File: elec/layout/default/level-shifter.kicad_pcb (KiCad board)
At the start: 2 copper layers, 225.7 x 100.8 mm, 0 parts

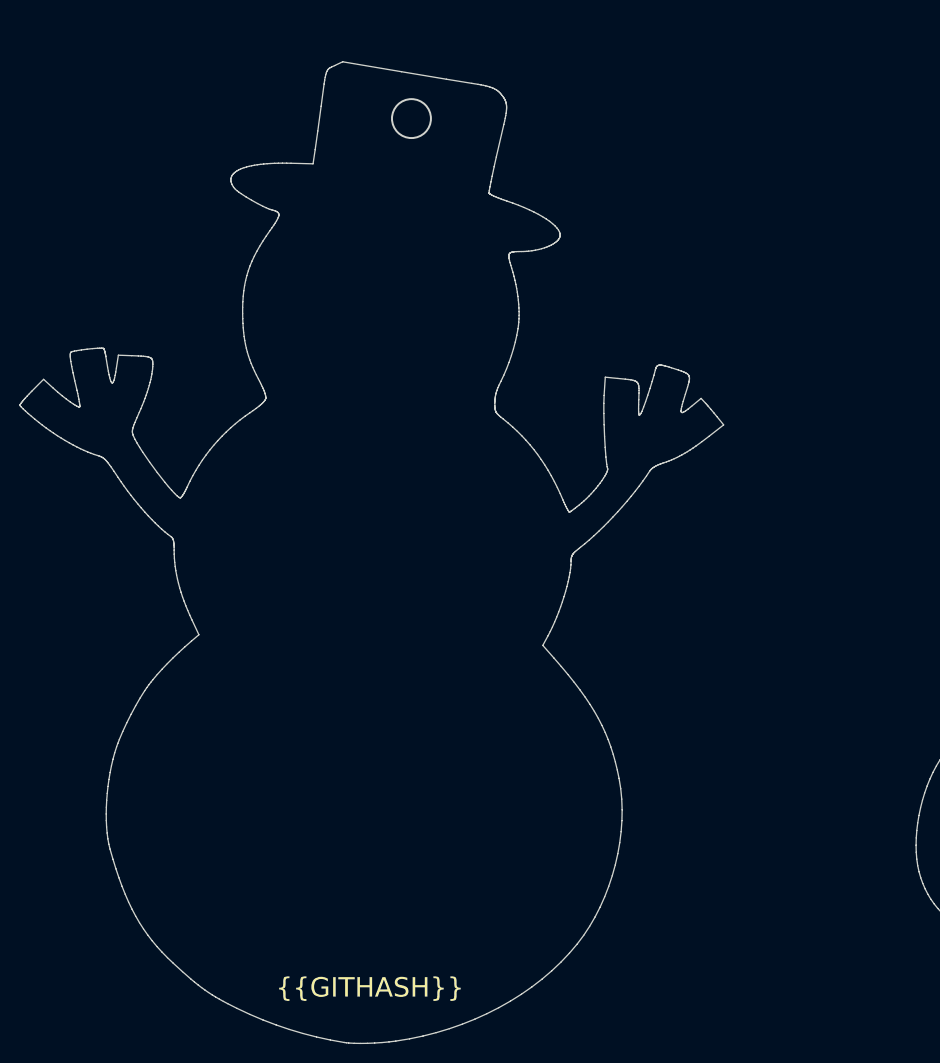
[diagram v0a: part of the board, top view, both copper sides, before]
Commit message: migrate to new project structure and add layout
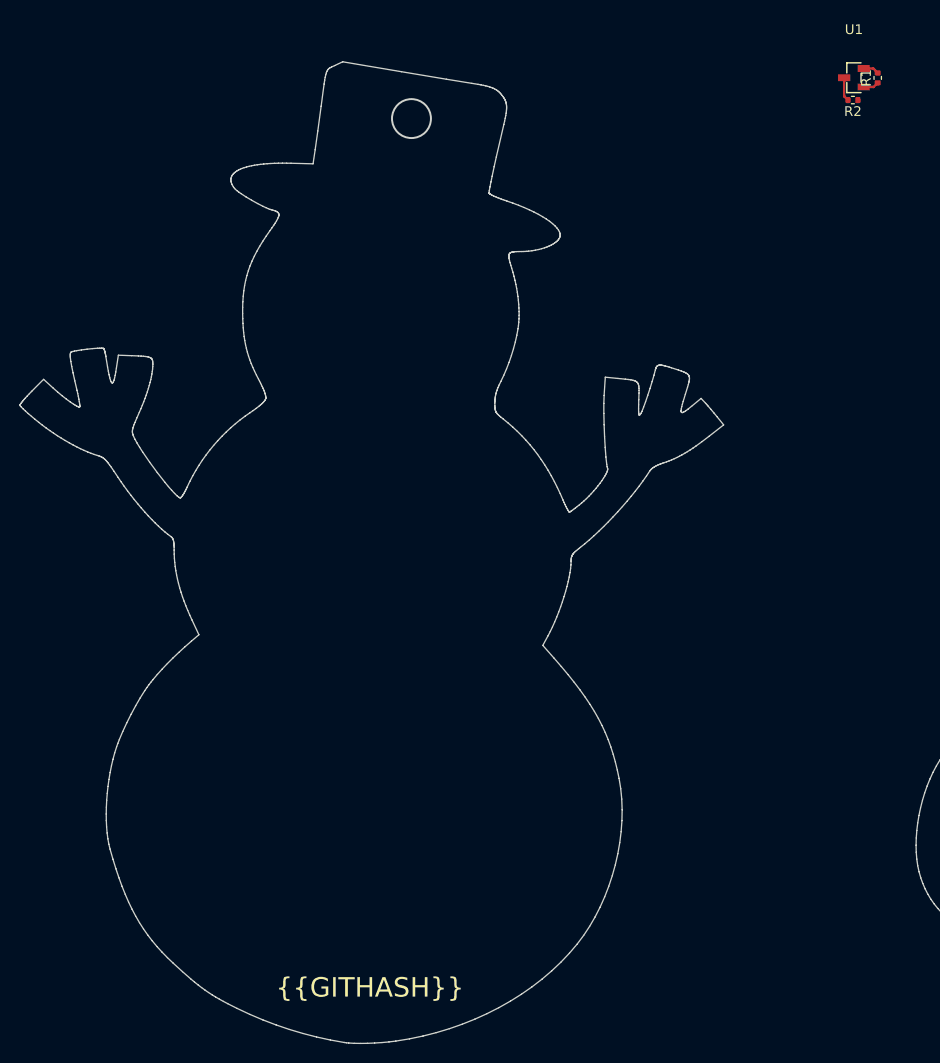
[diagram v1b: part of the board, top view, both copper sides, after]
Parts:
- added R1: Chip Resistor - Surface Mount 10KOhms ±5% 1/16W 0402 RoHS, lib:R0402, F.Cu at (124.1, 51.4)
- added R2: Chip Resistor - Surface Mount 10KOhms ±5% 1/16W 0402 RoHS, lib:R0402, F.Cu at (121.5, 53.7)
- added U1: , lib:SOT-23-3_L2.9-W1.3-P1.90-LS2.4-BR, F.Cu at (121.6, 51.4)
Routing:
- net hv_signal: track 0.00 -> 2.45 mm
- net lv_signal: track 0.00 -> 1.63 mm
- net vcc: track 0.00 -> 1.62 mm
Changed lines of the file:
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@@
   )
   (net 0 "")
+  (net 1 "vcc")
+  (net 2 "lv_signal")
+  (net 3 "hv_signal")
+  (net 4 "vcc-1")
+  (footprint "lib:R0402" (layer "F.Cu")
+    (at 124.058996 51.431563 90)
+    (descr "Resistor SMD 0402 (1005 Metric), square (rectangular) end terminal, IPC_7351 nominal, (Body size source: IPC-SM-782 page 72, https://www.pcb-3d.com/wordpress/wp-content/uploads/ipc-sm-782a_amendment_1_and_2.pdf), generated with kicad-footprint-generator")
+    (tags "resistor")
+    (attr smd)
+    (fp_text reference "R1" (at 0 -1.17 90) (layer "F.SilkS")
+        (effects (font (size 1 1) (thickness 0.15)))
+    )
+    (fp_text value "Chip Resistor - Surface Mount 10KOhms ±5% 1/16W 0402 RoHS" (at 0 1.17 90) (layer "F.Fab")
+        (effects (font (size 1 1) (thickness 0.15)))
+    )
+    (fp_text user "${REFERENCE}" (at 0 0 90) (layer "F.Fab")
+        (effects (font (size 0.26 0.26) (thickness 0.04)))
+    )
+    (fp_line (start -0.153641 -0.38) (end 0.153641 -0.38)
+      (stroke (width 0.12) (type solid)) (layer "F.SilkS"))
+    (fp_line (start -0.153641 0.38) (end 0.153641 0.38)
+      (stroke (width 0.12) (type solid)) (layer "F.SilkS"))
+    (fp_line (start -0.93 -0.47) (end 0.93 -0.47)
+      (stroke (width 0.05) (type solid)) (layer "F.CrtYd"))
+    (fp_line (start -0.93 0.47) (end -0.93 -0.47)
+      (stroke (width 0.05) (type solid)) (layer "F.CrtYd"))
+    (fp_line (start 0.93 -0.47) (end 0.93 0.47)
+      (stroke (width 0.05) (type solid)) (layer "F.CrtYd"))
+    (fp_line (start 0.93 0.47) (end -0.93 0.47)
+      (stroke (width 0.05) (type solid)) (layer "F.CrtYd"))
+    (fp_line (start -0.525 -0.27) (end 0.525 -0.27)
+      (stroke (width 0.1) (type solid)) (layer "F.Fab"))
+    (fp_line (start -0.525 0.27) (end -0.525 -0.27)
+      (stroke (width 0.1) (type solid)) (layer "F.Fab"))
+    (fp_line (start 0.525 -0.27) (end 0.525 0.27)
+      (stroke (width 0.1) (type solid)) (layer "F.Fab"))
+    (fp_line (start 0.525 0.27) (end -0.525 0.27)
+      (stroke (width 0.1) (type solid)) (layer "F.Fab"))
+    (pad "1" smd roundrect (at -0.51 0 90) (size 0.54 0.64) (layers "F.Cu" "F.Paste" "F.Mask") (roundrect_rratio 0.25)
+      (net 1 "vcc") (pintype "stereo"))
+    (pad "2" smd roundrect (at 0.51 0 90) (size 0.54 0.64) (layers "F.Cu" "F.Paste" "F.Mask") (roundrect_rratio 0.25)
+      (net 2 "lv_signal") (pintype "stereo"))
+    (model "${KICAD6_3DMODEL_DIR}/Resistor_SMD.3dshapes/R_0402_1005Metric.wrl"
+      (offset (xyz 0 0 0))
+      (scale (xyz 1 1 1))
+      (rotate (xyz 0 0 0))
+    )
+  )
+  (footprint "lib:SOT-23-3_L2.9-W1.3-P1.90-LS2.4-BR" (layer "F.Cu")
+    (at 121.615 51.415)
+    (attr smd)
+    (fp_text reference "U1" (at 0 -4.95) (layer "F.SilkS")
+        (effects (font (size 1 1) (thickness 0.15)))
+    )
+    (fp_text value "" (at 0 4.95) (layer "F.Fab")
+        (effects (font (size 1 1) (thickness 0.15)))
+    )
+    (fp_text user "${REFERENCE}" (at 0 0) (layer "F.Fab")
+        (effects (font (size 1 1) (thickness 0.15)))
+    )
+    (fp_line (start -0.73 -1.53) (end -0.73 -0.49)
+      (stroke (width 0.15) (type solid)) (layer "F.SilkS"))
+    (fp_line (start -0.73 1.53) (end -0.73 0.49)
+      (stroke (width 0.15) (type solid)) (layer "F.SilkS"))
+    (fp_line (start 0.73 -1.53) (end -0.73 -1.53)
+      (stroke (width 0.15) (type solid)) (layer "F.SilkS"))
+    (fp_line (start 0.73 -0.46) (end 0.73 0.46)
+      (stroke (width 0.15) (type solid)) (layer "F.SilkS"))
+    (fp_line (start 0.73 1.53) (end -0.73 1.53)
+      (stroke (width 0.15) (type solid)) (layer "F.SilkS"))
+    (fp_circle (center 1.46 1.1) (end 1.56 1.1)
+      (stroke (width 0.2) (type solid)) (fill none) (layer "Cmts.User"))
+    (fp_circle (center 1.2 1.45) (end 1.23 1.45)
+      (stroke (width 0.06) (type solid)) (fill none) (layer "F.Fab"))
+    (pad "1" smd rect (at 1 0.95) (size 1.25 0.7) (layers "F.Cu" "F.Paste" "F.Mask")
+      (net 1 "vcc") (pintype "stereo"))
+    (pad "2" smd rect (at 1 -0.95) (size 1.25 0.7) (layers "F.Cu" "F.Paste" "F.Mask")
+      (net 2 "lv_signal") (pintype "stereo"))
+    (pad "3" smd rect (at -1 0) (size 1.25 0.7) (layers "F.Cu" "F.Paste" "F.Mask")
+      (net 3 "hv_signal") (pintype "stereo"))
+    (model "/Users/narayanpowderly/Documents/atopile-workspace/blinky/.ato/level-shifter/elec/footprints/footprints.3dshapes/SOT-23-3P_L2.9-W1.3-H1.0-LS2.4-P0.95.wrl"
+      (offset (xyz -861.57 843.28 -0))
+      (scale (xyz 1 1 1))
+      (rotate (xyz 0 0 180))
+    )
+  )
+  (footprint "lib:R0402" (layer "F.Cu")
+    (at 121.508806 53.709823 180)
+    (descr "Resistor SMD 0402 (1005 Metric), square (rectangular) end terminal, IPC_7351 nominal, (Body size source: IPC-SM-782 page 72, https://www.pcb-3d.com/wordpress/wp-content/uploads/ipc-sm-782a_amendment_1_and_2.pdf), generated with kicad-footprint-generator")
+    (tags "resistor")
+    (attr smd)
+    (fp_text reference "R2" (at 0 -1.17) (layer "F.SilkS")
+        (effects (font (size 1 1) (thickness 0.15)))
+    )
+    (fp_text value "Chip Resistor - Surface Mount 10KOhms ±5% 1/16W 0402 RoHS" (at 0 1.17) (layer "F.Fab")
+        (effects (font (size 1 1) (thickness 0.15)))
+    )
+    (fp_text user "${REFERENCE}" (at 0 0) (layer "F.Fab")
+        (effects (font (size 0.26 0.26) (thickness 0.04)))
+    )
+    (fp_line (start -0.153641 -0.38) (end 0.153641 -0.38)
+      (stroke (width 0.12) (type solid)) (layer "F.SilkS"))
+    (fp_line (start -0.153641 0.38) (end 0.153641 0.38)
+      (stroke (width 0.12) (type solid)) (layer "F.SilkS"))
+    (fp_line (start -0.93 -0.47) (end 0.93 -0.47)
+      (stroke (width 0.05) (type solid)) (layer "F.CrtYd"))
+    (fp_line (start -0.93 0.47) (end -0.93 -0.47)
+      (stroke (width 0.05) (type solid)) (layer "F.CrtYd"))
+    (fp_line (start 0.93 -0.47) (end 0.93 0.47)
+      (stroke (width 0.05) (type solid)) (layer "F.CrtYd"))
+    (fp_line (start 0.93 0.47) (end -0.93 0.47)
+      (stroke (width 0.05) (type solid)) (layer "F.CrtYd"))
+    (fp_line (start -0.525 -0.27) (end 0.525 -0.27)
+      (stroke (width 0.1) (type solid)) (layer "F.Fab"))
+    (fp_line (start -0.525 0.27) (end -0.525 -0.27)
+      (stroke (width 0.1) (type solid)) (layer "F.Fab"))
+    (fp_line (start 0.525 -0.27) (end 0.525 0.27)
+      (stroke (width 0.1) (type solid)) (layer "F.Fab"))
+    (fp_line (start 0.525 0.27) (end -0.525 0.27)
+      (stroke (width 0.1) (type solid)) (layer "F.Fab"))
+    (pad "1" smd roundrect (at -0.51 0 180) (size 0.54 0.64) (layers "F.Cu" "F.Paste" "F.Mask") (roundrect_rratio 0.25)
+      (net 4 "vcc-1") (pintype "stereo"))
+    (pad "2" smd roundrect (at 0.51 0 180) (size 0.54 0.64) (layers "F.Cu" "F.Paste" "F.Mask") (roundrect_rratio 0.25)
+      (net 3 "hv_signal") (pintype "stereo"))
+    (model "${KICAD6_3DMODEL_DIR}/Resistor_SMD.3dshapes/R_0402_1005Metric.wrl"
+      (offset (xyz 0 0 0))
+      (scale (xyz 1 1 1))
+      (rotate (xyz 0 0 0))
+    )
+  )
   (gr_circle (center 225.62 81.79) (end 227.32 81.79)
     (stroke (width 0.1) (type solid)) (fill none) (layer "Edge.Cuts"))
@@
       (xy 69.100734 49.778315)
     )
-    (stroke (width 0) (type solid)) (fill none) (layer "Edge.Cuts"))
+    (stroke (width 0.1) (type solid)) (fill none) (layer "Edge.Cuts"))
   (gr_arc (start 261.62 113.79) (mid 260.448427 116.618427) (end 257.62 117.79)
     (stroke (width 0.1) (type solid)) (layer "Edge.Cuts"))
@@
     (effects (font (size 2 2) (thickness 0.1)) (justify left bottom))
   )
+  (segment (start 123.635559 52.365) (end 124.058996 51.941563) (width 0.25) (layer "F.Cu") (net 1))
+  (segment (start 122.615 52.365) (end 123.635559 52.365) (width 0.25) (layer "F.Cu") (net 1))
+  (segment (start 122.615 50.465) (end 123.602433 50.465) (width 0.25) (layer "F.Cu") (net 2))
+  (segment (start 123.602433 50.465) (end 124.058996 50.921563) (width 0.25) (layer "F.Cu") (net 2))
+  (segment (start 120.615 51.415) (end 120.615 53.326017) (width 0.25) (layer "F.Cu") (net 3))
+  (segment (start 120.615 53.326017) (end 120.998806 53.709823) (width 0.25) (layer "F.Cu") (net 3))
   (group "" (id 6c1ef9f7-0f34-47bb-ac1a-76df23fb396e)
     (members
